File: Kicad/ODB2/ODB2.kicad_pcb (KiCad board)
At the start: 4 copper layers, 83.9 x 76.5 mm, 183 parts, among them J4 RF2-04A-T-00-50-G, J5 RFM_Conn_Coaxial, U1 STM32F412ZGTx, U10 W25Q512JVEIQ, U2 TLV2371DBV, U3 74LV1T87GVH, U5 L76L-M33, U6 ICM-20948, U7 MS580301BA01-00

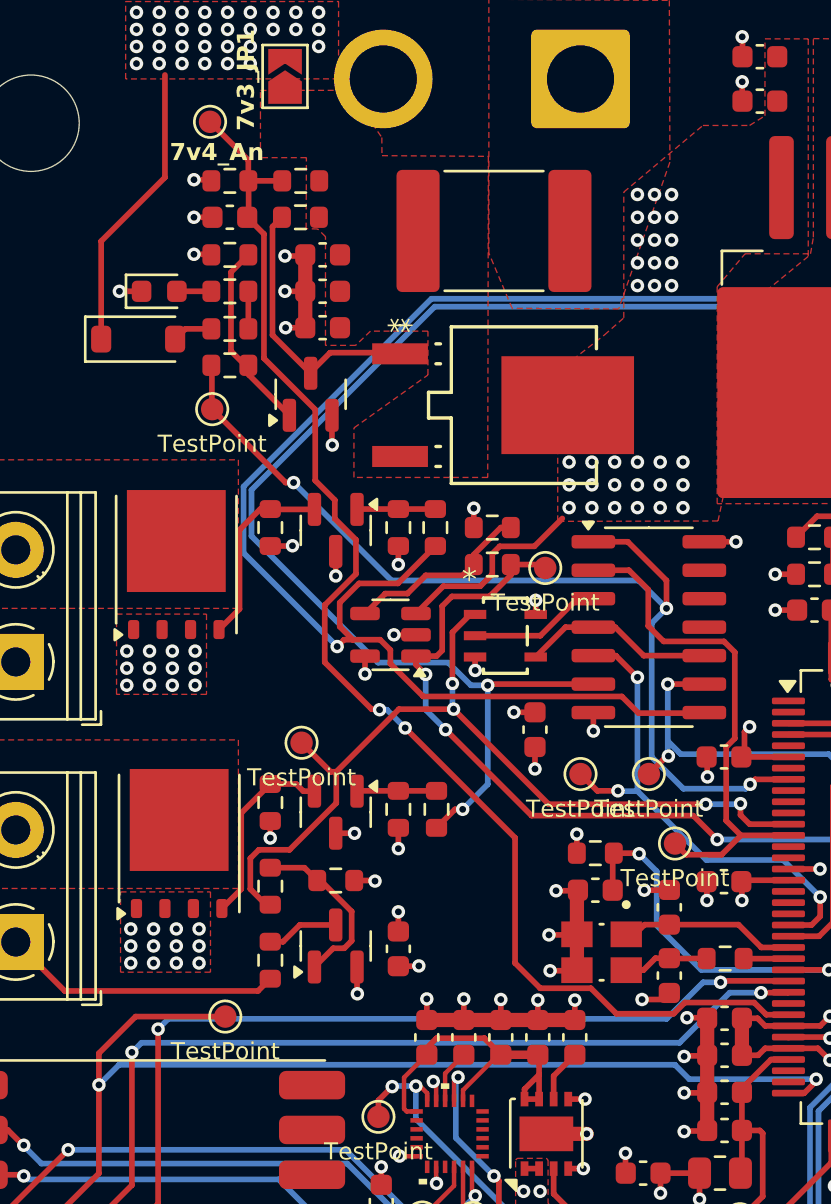
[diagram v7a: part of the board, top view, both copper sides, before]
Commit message: fixes + tests pads silkscreen
- vérifier W25Q512JVEIQ 3d model / footprint
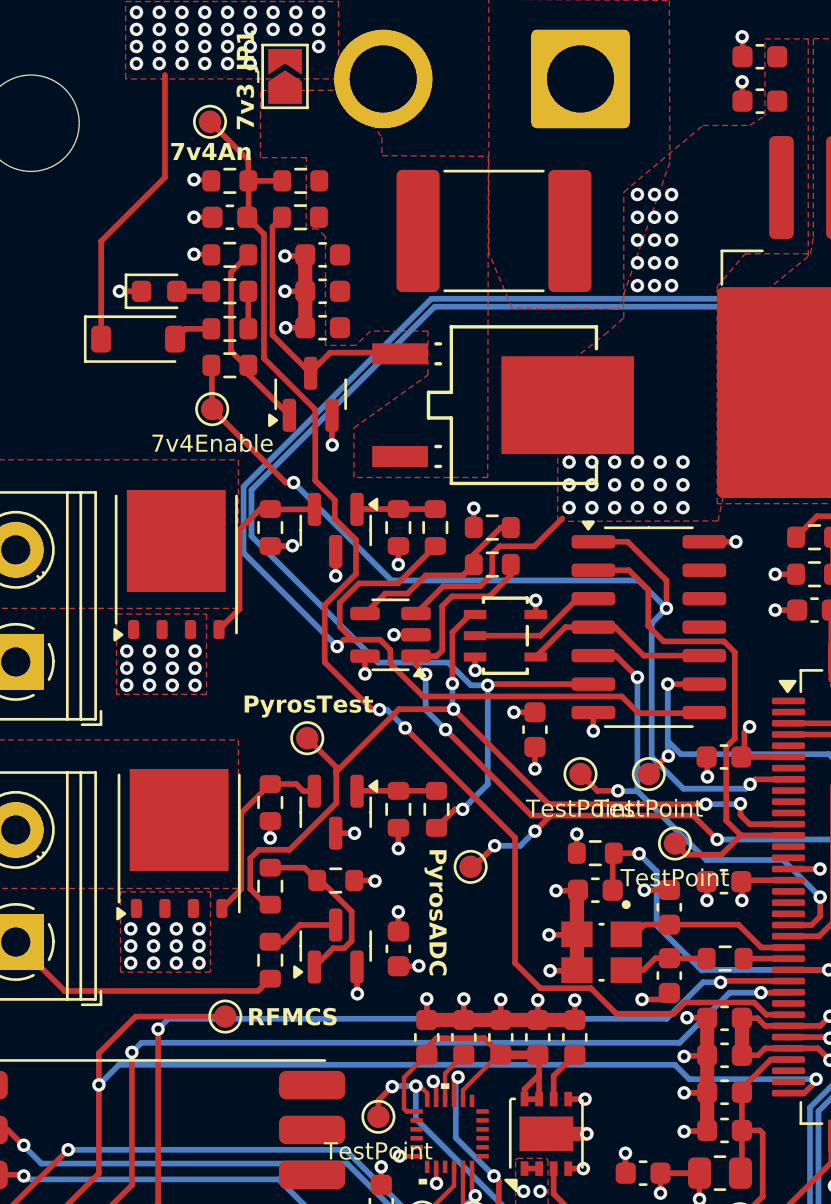
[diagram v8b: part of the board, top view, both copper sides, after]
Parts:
- TP21: value TestPoint -> 7v4Enable
- moved TP15 13.7 mm to (25.6, 39.1)
- moved TP22 0.33 mm to (18.3, 33.4)
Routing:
- net Pyros_ADC: track 46.8 -> 49.7 mm, vias 4 -> 6
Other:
- board text added: "7v4An"
- board text added: "Lukas Dupuis Samuel Gagnon Mathis Tremblay Victor Deschênes Brieuc Soriano-Lohéac"
- board text added: "PyrosADC"
- board text added: "PyrosTest"
- board text added: "RFMCS"
- board text removed: "7v4_An"
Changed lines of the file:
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@@
 			(layer "F.Fab")
 		)
-		(fp_text user "*"
-			(at -3.560001 5.5245 90)
-			(layer "F.SilkS")
-			(effects
-				(font
-					(size 1 1)
-					(thickness 0.15)
-				)
-			)
-		)
-		(fp_text user "*"
-			(at -3.560001 5.5245 -90)
-			(unlocked yes)
-			(layer "F.SilkS")
-			(effects
-				(font
-					(size 1 1)
-					(thickness 0.15)
-				)
-			)
-		)
-		(fp_text user "*"
-			(at -2.29 2.8575 90)
-			(layer "F.Fab")
-			(effects
-				(font
-					(size 1 1)
-					(thickness 0.15)
-				)
-			)
-		)
 		(fp_text user "${REFERENCE}"
 			(at 0 0 -90)
@@
 			)
 		)
-		(fp_text user "*"
-			(at -2.29 2.8575 -90)
-			(unlocked yes)
-			(layer "F.Fab")
-			(effects
-				(font
-					(size 1 1)
-					(thickness 0.15)
-				)
-			)
-		)
 		(pad "1" smd rect
 			(at -2.29 5.5245 270)
@@
 			(layer "F.Fab")
 		)
-		(fp_text user "*"
-			(at -1.60655 -2.4994 0)
-			(unlocked yes)
-			(layer "F.SilkS")
-			(effects
-				(font
-					(size 1 1)
-					(thickness 0.15)
-				)
-			)
-		)
-		(fp_text user "*"
-			(at -1.60655 -2.4994 0)
-			(layer "F.SilkS")
-			(effects
-				(font
-					(size 1 1)
-					(thickness 0.15)
-				)
-			)
-		)
-		(fp_text user "*"
-			(at -0.5969 -1.4072 0)
-			(unlocked yes)
-			(layer "F.Fab")
-			(effects
-				(font
-					(size 1 1)
-					(thickness 0.15)
-				)
-			)
-		)
 		(fp_text user "${REFERENCE}"
 			(at 0 0 0)
@@
 			)
 		)
-		(fp_text user "*"
-			(at -0.5969 -1.4072 0)
-			(layer "F.Fab")
-			(effects
-				(font
-					(size 1 1)
-					(thickness 0.15)
-				)
-			)
-		)
 		(pad "1" smd rect
 			(at -1.35255 -0.950001)
@@
 			)
 		)
-		(property "Value" "TestPoint"
+		(property "Value" "7v4Enable"
 			(at 0 1.55 0)
 			(layer "F.SilkS")
@@
 	(footprint "TestPoint:TestPoint_Pad_D1.0mm"
 		(layer "F.Cu")
-		(at 28.9052 25.8064)
+		(at 25.5778 39.1414)
 		(descr "SMD pad as test Point, diameter 1.0mm")
 		(tags "test point SMD pad")
@@
 			(at 0 1.55 0)
 			(layer "F.SilkS")
+			(hide yes)
 			(effects
 				(font
@@
 			(at 0 1.55 0)
 			(layer "F.SilkS")
+			(hide yes)
 			(effects
 				(font
@@
 	(footprint "TestPoint:TestPoint_Pad_D1.0mm"
 		(layer "F.Cu")
-		(at 18.034 33.6042)
+		(at 18.288 33.401)
 		(descr "SMD pad as test Point, diameter 1.0mm")
 		(tags "test point SMD pad")
@@
 			(at 0 1.55 0)
 			(layer "F.SilkS")
+			(hide yes)
 			(effects
 				(font
@@
 		(layer "Edge.Cuts")
 	)
+	(gr_text "Lukas Dupuis\nSamuel Gagnon\nMathis Tremblay\nVictor Deschênes\nBrieuc Soriano-Lohéac"
+		(at 80.01 20.32 90)
+		(layer "B.SilkS")
+		(effects
+			(font
+				(size 0.762 0.762)
+				(thickness 0.127)
+				(bold yes)
+			)
+			(justify left bottom mirror)
+		)
+	)
+	(gr_text "PyrosTest"
+		(at 15.4 32.35 0)
+		(layer "F.SilkS")
+		(effects
+			(font
+				(size 0.762 0.762)
+				(thickness 0.127)
+				(bold yes)
+			)
+			(justify left bottom)
+		)
+	)
+	(gr_text "RFMCS"
+		(at 15.6 46.3 0)
+		(layer "F.SilkS")
+		(effects
+			(font
+				(size 0.762 0.762)
+				(thickness 0.127)
+				(bold yes)
+			)
+			(justify left bottom)
+		)
+	)
+	(gr_text "PyrosADC"
+		(at 23.65 38.3 -90)
+		(layer "F.SilkS")
+		(effects
+			(font
+				(size 0.762 0.762)
+				(thickness 0.127)
+				(bold yes)
+			)
+			(justify left bottom)
+		)
+	)
 	(gr_text "7v3_JP1"
 		(at 16 6.3 90)
@@
 		)
 	)
-	(gr_text "7v4_An"
+	(gr_text "7v4An"
 		(at 12.15 7.7 0)
 		(layer "F.SilkS")
@@
 	)
 	(segment
-		(start 28.7528 25.654)
-		(end 28.9052 25.8064)
-		(width 0.254)
-		(layer "F.Cu")
-		(net 76)
-	)
-	(segment
 		(start 23.1394 29.7384)
 		(end 24.0588 29.7384)
@@
 	)
 	(segment
-		(start 27.368 25.654)
-		(end 28.7528 25.654)
+		(start 24.7396 27.0764)
+		(end 26.4206 27.0764)
 		(width 0.254)
 		(layer "F.Cu")
@@
 	)
 	(segment
-		(start 24.7396 27.0764)
-		(end 26.4206 27.0764)
+		(start 45.168999 41.231999)
+		(end 45.168999 51.1501)
 		(width 0.254)
 		(layer "F.Cu")
@@
 	)
 	(segment
-		(start 45.168999 41.231999)
-		(end 45.168999 51.1501)
+		(start 28.45 37.55)
+		(end 29.1446 36.8554)
 		(width 0.254)
 		(layer "F.Cu")
@@
 	)
 	(segment
-		(start 28.2956 36.8554)
-		(end 35.5092 36.8554)
+		(start 29.1446 36.8554)
+		(end 29.15 36.8554)
 		(width 0.254)
 		(layer "F.Cu")
@@
 	)
 	(segment
+		(start 29.15 36.8554)
+		(end 35.5092 36.8554)
+		(width 0.254)
+		(layer "F.Cu")
+		(net 76)
+	)
+	(segment
 		(start 42.2656 38.3286)
 		(end 45.168999 41.231999)
@@
 	)
 	(segment
+		(start 25.5778 39.1414)
+		(end 25.7086 39.1414)
+		(width 0.254)
+		(layer "F.Cu")
+		(net 76)
+	)
+	(segment
+		(start 25.7086 39.1414)
+		(end 26.65 38.2)
+		(width 0.254)
+		(layer "F.Cu")
+		(net 76)
+	)
+	(segment
 		(start 24.0588 29.7384)
 		(end 24.3078 29.4894)
@@
 	)
 	(segment
+		(start 28.2956 36.8554)
+		(end 29.15 36.8554)
+		(width 0.254)
+		(layer "F.Cu")
+		(net 76)
+	)
+	(segment
 		(start 23.1394 29.7384)
 		(end 23.1394 30.1244)
@@
 	)
 	(via
+		(at 28.45 37.55)
+		(size 0.6)
+		(drill 0.3)
+		(layers "F.Cu" "B.Cu")
+		(net 76)
+	)
+	(via
+		(at 26.65 38.2)
+		(size 0.6)
+		(drill 0.3)
+		(layers "F.Cu" "B.Cu")
+		(net 76)
+	)
+	(via
 		(at 24.4602 33.02)
 		(size 0.6)
@@
 	)
 	(segment
+		(start 27.8 38.2)
+		(end 28.45 37.55)
+		(width 0.254)
+		(layer "B.Cu")
+		(net 76)
+	)
+	(segment
 		(start 23.5712 32.131)
 		(end 24.4602 33.02)
@@
 	)
 	(segment
+		(start 26.65 38.2)
+		(end 27.8 38.2)
+		(width 0.254)
+		(layer "B.Cu")
+		(net 76)
+	)
+	(segment
 		(start 36.576 37.9222)
 		(end 41.8592 37.9222)
@@
 	)
 	(segment
-		(start 18.034 33.6042)
-		(end 19.3294 34.8996)
+		(start 19.5834 34.6964)
+		(end 18.288 33.401)
 		(width 0.254)
 		(layer "F.Cu")
@@
 	)
 	(segment
-		(start 15.748 38.7604)
-		(end 15.748 40.132)
+		(start 19.5834 34.8996)
+		(end 19.5834 34.6964)
 		(width 0.254)
 		(layer "F.Cu")
@@
 	)
 	(segment
-		(start 19.5834 35.0012)
-		(end 19.5834 36.2966)
+		(start 15.748 38.7604)
+		(end 15.748 40.132)
 		(width 0.254)
 		(layer "F.Cu")
@@
 	)
 	(segment
-		(start 19.3294 34.8996)
-		(end 19.5834 34.8996)
+		(start 19.5834 35.0012)
+		(end 19.5834 36.2966)
 		(width 0.254)
 		(layer "F.Cu")
